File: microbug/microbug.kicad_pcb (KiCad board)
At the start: 2 copper layers, 31.7 x 38.1 mm, 26 parts, among them J1 Conn_01x03, J2 Conn_01x03, J3 Conn_01x02, M1 Motor_DC, M2 Motor_DC, U1 ATtiny1616-S, U2 QRE1113GR, U4 QRE1113GR, U5 TC78H660FNG

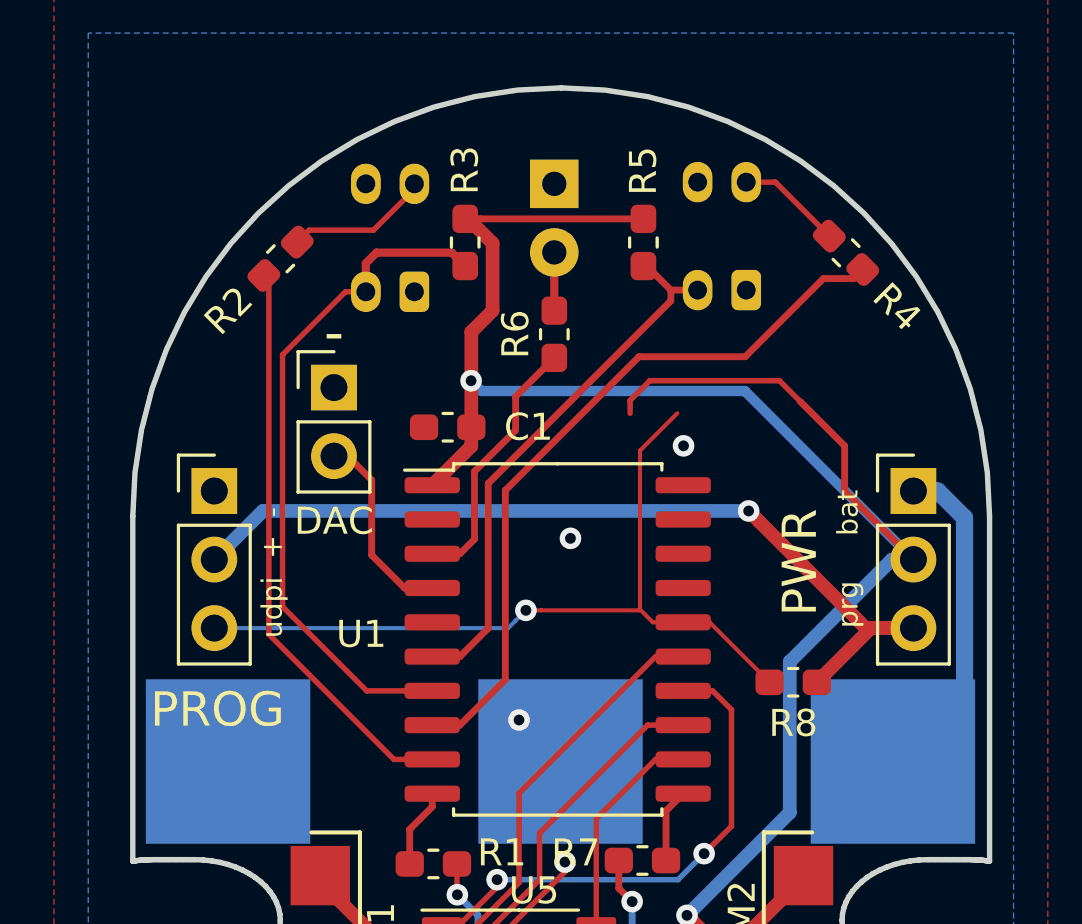
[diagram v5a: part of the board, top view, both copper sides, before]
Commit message: fixed programming header stuff and qre111 symbol stuff
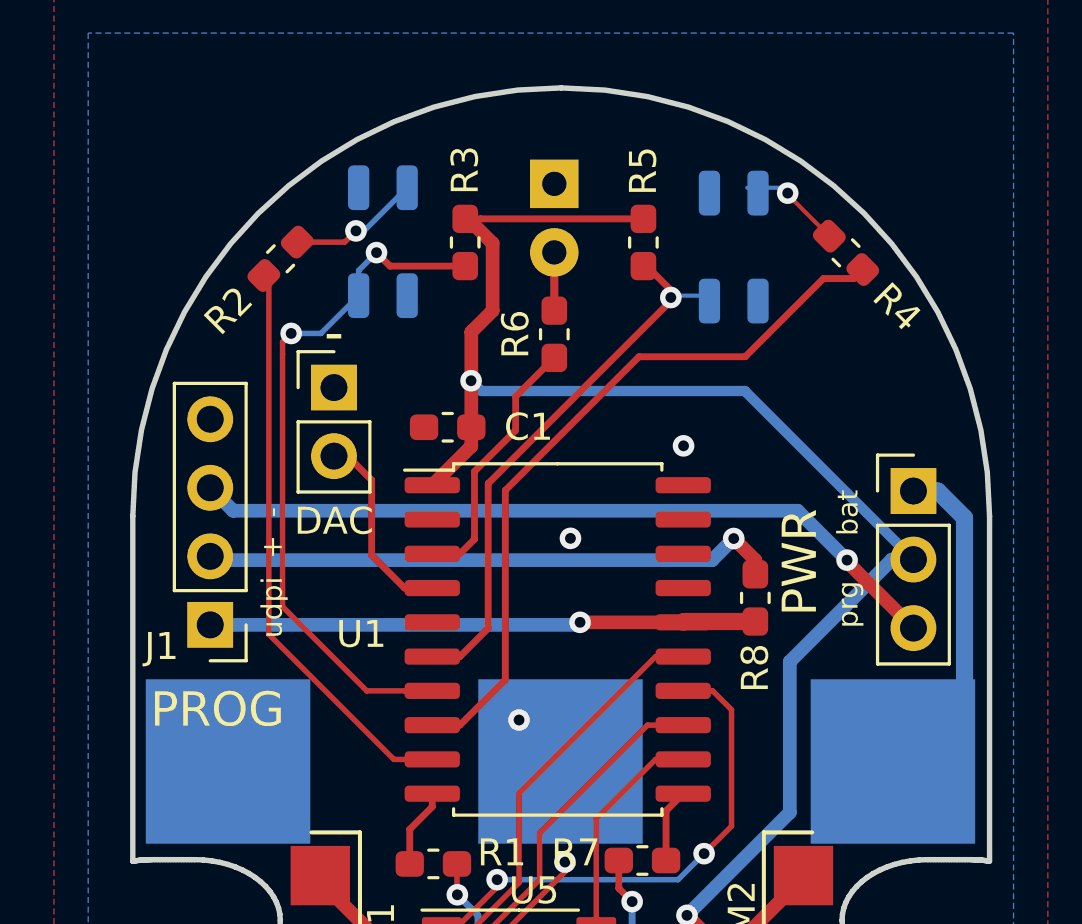
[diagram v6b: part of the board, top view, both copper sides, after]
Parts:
- removed U4: QRE1113GR, OptoDevice:Everlight_ITR8307F43
- added U3: QRE1113GR, OptoDevice:OnSemi_CASE100CY, B.Cu at (80.6, 42.8)
- J1: value Conn_01x03 -> Conn_01x04; footprint Connector_PinHeader_2.54mm:PinHeader_1x03_P2.54mm_Vertical -> Connector_PinHeader_2.54mm:PinHeader_1x04_P2.54mm_Vertical
- U2: footprint OptoDevice:Everlight_ITR8307F43 -> OptoDevice:OnSemi_CASE100CY
- moved J1 4.96 mm to (61.2, 56.8), turned to 180 degrees
- moved R8 3.43 mm to (81.4, 55.8), turned to -90 degrees
- moved U2 2.19 mm to (67.6, 42.6)
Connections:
- J1 pad 1: GND -> /UDPI
- J1 pad 3: /UDPI -> Net-(J1-Pad3)
- J2 pad 3: Net-(J1-Pad2) -> Net-(J1-Pad3)
- R8 pad 1: /UDPI -> Net-(J1-Pad2)
- R8 pad 2: Net-(J1-Pad2) -> /UDPI
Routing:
- net Net-(J1-Pad3): track 0.00 -> 28.2 mm, vias 0 -> 1
- net +3V3: track 85.3 -> 70.3 mm
- net Net-(J1-Pad2): track 32.9 -> 21.4 mm
- net /UDPI: track 29.9 -> 20.3 mm
- net /IR1: track 22.4 -> 21.3 mm
- net Net-(R2-Pad2): track 5.35 -> 4.91 mm, vias 0 -> 1
- net Net-(R4-Pad2): track 4.13 -> 3.82 mm, vias 0 -> 1
- net /OUT1: track 27.3 -> 27.5 mm, vias 0 -> 2
- net /OUT2: track 20.2 -> 20.3 mm, vias 0 -> 1

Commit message: pulled motor driver pin 15 up
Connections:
- U5 pad 15: unconnected-(U5-Pad15) -> +3V3
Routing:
- net +3V3: track 70.3 -> 73.0 mm
